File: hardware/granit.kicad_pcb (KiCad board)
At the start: 4 copper layers, 92 x 100 mm, 112 parts, among them IC1 ASM1061, J1 12V Barrel, J2 12V Screw Terminal, J3 RJ45_RB1-125B8G1A, J6 Conn_01x02, J7 USB_C_Receptacle_USB2.0_14P, J8 Conn_01x03, J9 SATA_22pin, Q1 FDS4435BZ, Q2 FDS4435BZ, Q3 FDS4435BZ, Q4 2N7002, Q5 2N7002, Q6 2N7002, SW1 SW_Push, U1 NCP1117-3.3_SOT223, U2 AP64501SP-13, U3 74AHCT1G125, U4 DS3231MZ, U5 USBLC6-2SC6, U6 74AHCT1G32, Y1 Crystal

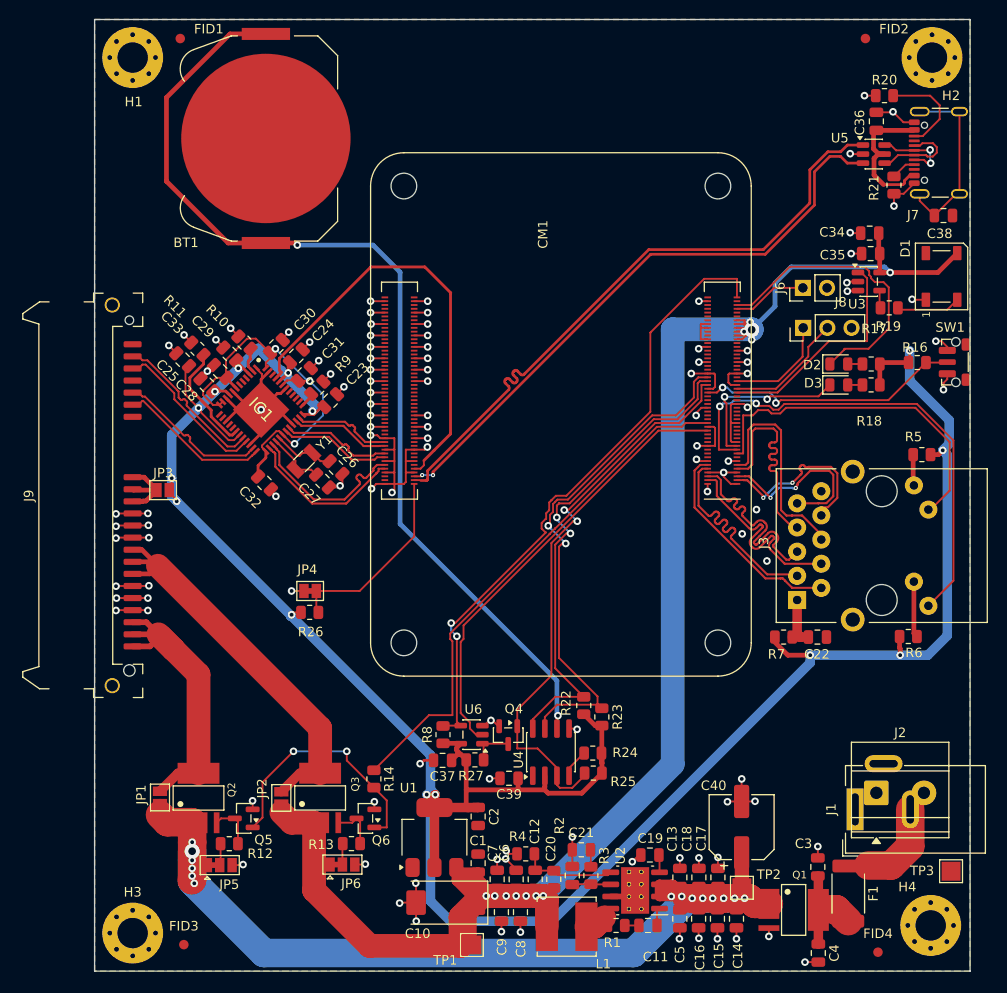
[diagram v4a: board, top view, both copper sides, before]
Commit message: Add comments to DRC exclusions
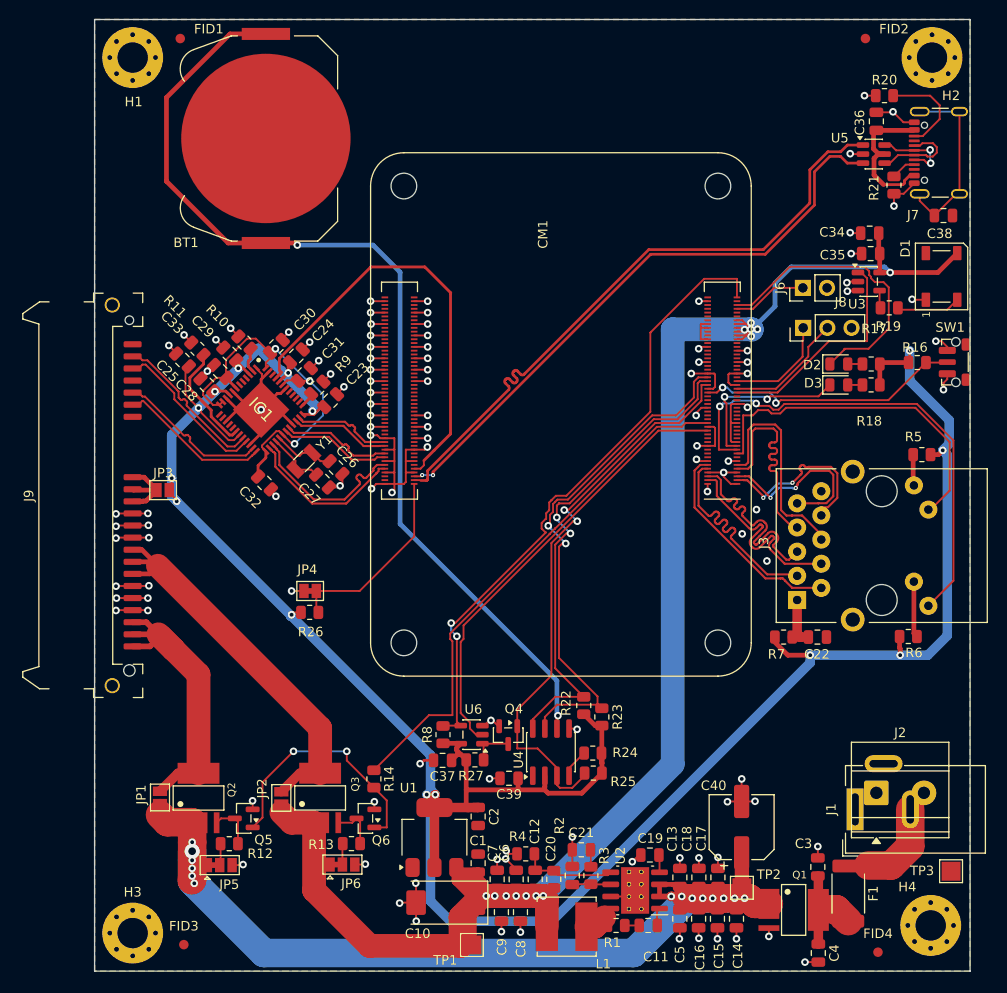
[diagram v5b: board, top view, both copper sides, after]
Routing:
- net +12VP: track 102.6 -> 96.7 mm
- net +5VP: track 190.0 -> 188.5 mm, vias 12 -> 13
- net GND: track 212.0 -> 212.9 mm
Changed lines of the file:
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@@
 	(footprint "Capacitor_SMD:C_0805_2012Metric"
 		(layer "F.Cu")
-		(at 29.25 55.75 135)
+		(at 29.23 55.78 135)
 		(descr "Capacitor SMD 0805 (2012 Metric), square (rectangular) end terminal, IPC-7351 nominal, (Body size source: IPC-SM-782 page 76, https://www.pcb-3d.com/wordpress/wp-content/uploads/ipc-sm-782a_amendment_1_and_2.pdf, https://docs.google.com/spreadsheets/d/1BsfQQcO9C6DZCsRaXUlFlo91Tg2WpOkGARC1WS5S8t0/edit?usp=sharing)")
 		(tags "capacitor")
@@
 	(footprint "Capacitor_SMD:C_0805_2012Metric"
 		(layer "F.Cu")
-		(at 78.15 115.199999)
+		(at 78.18 115.199999)
 		(descr "Capacitor SMD 0805 (2012 Metric), square (rectangular) end terminal, IPC-7351 nominal, (Body size source: IPC-SM-782 page 76, https://www.pcb-3d.com/wordpress/wp-content/uploads/ipc-sm-782a_amendment_1_and_2.pdf, https://docs.google.com/spreadsheets/d/1BsfQQcO9C6DZCsRaXUlFlo91Tg2WpOkGARC1WS5S8t0/edit?usp=sharing)")
 		(tags "capacitor")
@@
 	)
 	(segment
+		(start 76.165 112.154106)
+		(end 76.8 111.519106)
+		(width 0.2)
+		(layer "F.Cu")
+		(net "GND")
+	)
+	(segment
 		(start 83.675344 54.4)
 		(end 83.479024 54.59632)
@@
 	)
 	(segment
+		(start 74.2375 112.154106)
+		(end 76.165 112.154106)
+		(width 0.2)
+		(layer "F.Cu")
+		(net "GND")
+	)
+	(segment
 		(start 52.7 66.4)
 		(end 53.58 66.4)
@@
 	)
 	(segment
-		(start 74.2375 112.154106)
-		(end 76.165 112.154106)
-		(width 0.6)
-		(layer "F.Cu")
-		(net "GND")
-	)
-	(segment
 		(start 99.45 42.45)
 		(end 99.4 42.4)
@@
 	)
 	(segment
-		(start 88.3 52.1)
-		(end 88.8 52.6)
-		(width 0.2)
-		(layer "F.Cu")
-		(net "+5VP")
-	)
-	(segment
 		(start 88.425 53.225)
-		(end 89.05 52.6)
+		(end 88.825 52.825)
 		(width 0.2)
 		(layer "F.Cu")
@@
 	)
 	(segment
-		(start 87.5 51.6)
-		(end 88.3 51.6)
+		(start 88.975 52.675)
+		(end 89.05 52.6)
 		(width 0.2)
 		(layer "F.Cu")
@@
 	)
 	(segment
-		(start 88.2 52)
-		(end 88.3 52.1)
-		(width 0.2)
+		(start 64.05 112.1)
+		(end 61.15 112.1)
+		(width 2.5)
 		(layer "F.Cu")
 		(net "+5VP")
 	)
 	(segment
-		(start 64.05 112.1)
-		(end 61.15 112.1)
-		(width 2.5)
+		(start 88.05 51.6)
+		(end 88.45 52)
+		(width 0.2)
 		(layer "F.Cu")
 		(net "+5VP")
@@
 	)
 	(segment
+		(start 87.5 52)
+		(end 88.45 52)
+		(width 0.2)
+		(layer "F.Cu")
+		(net "+5VP")
+	)
+	(segment
 		(start 63.25 112.1)
 		(end 62.05 112.1)
@@
 	)
 	(segment
-		(start 87.5 52.4)
-		(end 88.45 52.4)
-		(width 0.2)
-		(layer "F.Cu")
-		(net "+5VP")
-	)
-	(segment
 		(start 103.6 46.587501)
 		(end 108.612499 46.587501)
@@
 	(segment
 		(start 88.85 52.8)
-		(end 89.05 52.6)
+		(end 88.975 52.675)
 		(width 0.2)
 		(layer "F.Cu")
@@
 	)
 	(segment
+		(start 88.1 52.8)
+		(end 88.3 52.6)
+		(width 0.2)
+		(layer "F.Cu")
+		(net "+5VP")
+	)
+	(segment
+		(start 88.1 52.4)
+		(end 88.3 52.6)
+		(width 0.2)
+		(layer "F.Cu")
+		(net "+5VP")
+	)
+	(segment
 		(start 60.02 109.879999)
 		(end 60.3 109.599999)
@@
 	)
 	(segment
-		(start 87.5 52)
-		(end 88.2 52)
-		(width 0.2)
-		(layer "F.Cu")
-		(net "+5VP")
-	)
-	(segment
 		(start 60.02 111.15)
 		(end 60.02 109.879999)
@@
 	)
 	(segment
-		(start 88.8 52.6)
-		(end 89.05 52.6)
-		(width 0.2)
-		(layer "F.Cu")
-		(net "+5VP")
-	)
-	(segment
 		(start 43.065 104.4)
 		(end 40.7 104.4)
@@
 	)
 	(segment
-		(start 87.5 52.8)
-		(end 88.85 52.8)
-		(width 0.2)
-		(layer "F.Cu")
-		(net "+5VP")
-	)
-	(segment
 		(start 102.499999 46.575002)
 		(end 102.499999 44.6)
@@
 	)
 	(segment
-		(start 88.3 51.6)
-		(end 88.3 51.85)
+		(start 87.5 53.2)
+		(end 88.45 53.2)
 		(width 0.2)
 		(layer "F.Cu")
@@
 	)
 	(segment
-		(start 87.5 53.2)
-		(end 88.45 53.2)
+		(start 88.825 52.825)
+		(end 89.05 52.6)
 		(width 0.2)
 		(layer "F.Cu")
@@
 	)
 	(segment
-		(start 88.3 51.85)
+		(start 87.5 52.4)
+		(end 88.1 52.4)
+		(width 0.2)
+		(layer "F.Cu")
+		(net "+5VP")
+	)
+	(segment
+		(start 88.45 52)
 		(end 89.05 52.6)
 		(width 0.2)
@@
 	)
 	(segment
+		(start 87.5 51.6)
+		(end 88.05 51.6)
+		(width 0.2)
+		(layer "F.Cu")
+		(net "+5VP")
+	)
+	(segment
+		(start 87.5 52.8)
+		(end 88.1 52.8)
+		(width 0.2)
+		(layer "F.Cu")
+		(net "+5VP")
+	)
+	(segment
 		(start 102.399999 42.45)
 		(end 102.399999 44.5)
@@
 	)
 	(via
-		(at 89.05 52.6)
-		(size 1.6)
-		(drill 0.8)
-		(layers "F.Cu" "B.Cu")
-		(net "+5VP")
-	)
-	(via
-		(at 88.9 51.8)
+		(at 88.975 51.875)
 		(size 0.8)
 		(drill 0.4)
@@
 	)
 	(via
-		(at 88.25 52.8)
+		(at 88.3 52.6)
 		(size 0.8)
 		(drill 0.4)
@@
 	)
 	(via
+		(at 88.95 52.55)
+		(size 0.8)
+		(drill 0.4)
+		(layers "F.Cu" "B.Cu")
+		(net "+5VP")
+	)
+	(via
 		(at 63.25 112.1)
 		(size 0.8)
@@
 	)
 	(via
-		(at 89.05 53.650003)
+		(at 89.65 52.55)
+		(size 0.8)
+		(drill 0.4)
+		(layers "F.Cu" "B.Cu")
+		(net "+5VP")
+	)
+	(via
+		(at 89 53.3)
 		(size 0.8)
 		(drill 0.4)
@@
 	)
 	(segment
+		(start 89.6 52.05)
+		(end 91.5 50.15)
+		(width 0.5)
+		(layer "B.Cu")
+		(net "+5VP")
+	)
+	(segment
 		(start 93.2 46)
 		(end 103.012499 46)
@@
 	(segment
 		(start 89.05 52.6)
-		(end 91.5 50.15)
+		(end 89.6 52.05)
 		(width 0.5)
 		(layer "B.Cu")
@@
 	)
 	(segment
+		(start 88.95 52.55)
+		(end 89.05 52.55)
+		(width 2.5)
+		(layer "B.Cu")
+		(net "+5VP")
+	)
+	(segment
 		(start 103.012499 46)
 		(end 103.6 46.587501)
@@
 	(segment
 		(start 80.75 52.55)
-		(end 89.05 52.55)
+		(end 88.95 52.55)
 		(width 2.5)
 		(layer "B.Cu")
@@
 	(segment
 		(start 80.784106 110.884106)
-		(end 81.2 111.3)
-		(width 1)
+		(end 82.25 112.35)
+		(width 0.5)
 		(layer "F.Cu")
 		(net "+12VP")
@@
 	)
 	(segment
-		(start 80.6325 110.884106)
-		(end 80.784106 110.884106)
-		(width 1)
-		(layer "F.Cu")
-		(net "+12VP")
-	)
-	(segment
-		(start 79.3625 110.884106)
-		(end 79.3625 112.154106)
-		(width 1)
-		(layer "F.Cu")
-		(net "+12VP")
-	)
-	(segment
 		(start 30.2275 104.35)
 		(end 30.285 104.4075)
@@
 	)
 	(segment
-		(start 81.2 111.521606)
-		(end 81.2 111.3)
-		(width 1)
-		(layer "F.Cu")
-		(net "+12VP")
-	)
-	(segment
-		(start 79.3625 110.884106)
-		(end 80.6325 110.884106)
-		(width 1)
-		(layer "F.Cu")
-		(net "+12VP")
-	)
-	(segment
 		(start 82.8 112.35)
 		(end 82.25 112.35)
@@
 	)
 	(segment
-		(start 80.6 112.121606)
-		(end 81.2 111.521606)
-		(width 1)
+		(start 79.3625 110.884106)
+		(end 79.3625 112.154106)
+		(width 0.5)
 		(layer "F.Cu")
 		(net "+12VP")
@@
 	)
 	(segment
-		(start 79.3625 112.154106)
-		(end 79.45 112.154106)
-		(width 1)
-		(layer "F.Cu")
-		(net "+12VP")
-	)
-	(segment
 		(start 30.25 110.4)
 		(end 30.25 110)
@@
 	)
 	(segment
-		(start 79.3625 112.154106)
-		(end 80.6325 110.884106)
-		(width 1)
-		(layer "F.Cu")
-		(net "+12VP")
-	)
-	(segment
 		(start 86.1 112.35)
 		(end 84.95 112.35)
@@
 	)
 	(segment
-		(start 81.2 111.3)
-		(end 82.25 112.35)
-		(width 1)
-		(layer "F.Cu")
-		(net "+12VP")
-	)
-	(segment
 		(start 80.6 112.121606)
 		(end 80.6 112.154106)
@@
 	(segment
 		(start 79.3625 110.884106)
-		(end 80.6 112.121606)
-		(width 1)
-		(layer "F.Cu")
-		(net "+12VP")
-	)
-	(segment
-		(start 79.45 112.154106)
-		(end 80.6 112.154106)
-		(width 1)
+		(end 80.784106 110.884106)
+		(width 0.5)
 		(layer "F.Cu")
 		(net "+12VP")

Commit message: Connect mounting holes H1-H4 to GND
- Change symbols from MountingHole to MountingHole_Pad
- Wire pad to GND for chassis ground through metal standoffs
- Update PCB from schematic to sync nets and fields
- ERC clean, 0 schematic parity issues
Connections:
- H1 pad 1: (no net) -> GND
- H2 pad 1: (no net) -> GND
- H3 pad 1: (no net) -> GND
- H4 pad 1: (no net) -> GND
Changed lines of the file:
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@@
 			)
 		)
-		(property "Description" "Mounting Hole without connection"
+		(property "Description" "Mounting Hole with connection"
 			(at 0 0 0)
 			(layer "F.Fab")
@@
 			)
 		)
-		(property ki_fp_filters "MountingHole*")
+		(property ki_fp_filters "MountingHole*Pad*")
 		(sheetname "/")
 		(sheetfile "granit.kicad_sch")
+		(units
+			(unit
+				(name "A")
+				(pins "1")
+			)
+		)
 		(attr exclude_from_bom)
 		(duplicate_pad_numbers_are_jumpers no)
@@
 			(layers "*.Cu" "*.Mask")
 			(remove_unused_layers no)
+			(net "GND")
+			(pinfunction "1_1")
+			(pintype "input")
 			(zone_connect 2)
 		)
@@
 			(layers "*.Cu" "*.Mask")
 			(remove_unused_layers no)
+			(net "GND")
+			(pinfunction "1_1")
+			(pintype "input")
 			(zone_connect 2)
 		)
@@
 			(layers "*.Cu" "*.Mask")
 			(remove_unused_layers no)
+			(net "GND")
+			(pinfunction "1_1")
+			(pintype "input")
 			(zone_connect 2)
 		)
@@
 			(layers "*.Cu" "*.Mask")
 			(remove_unused_layers no)
+			(net "GND")
+			(pinfunction "1_1")
+			(pintype "input")
 			(zone_connect 2)
 		)
@@
 			(layers "*.Cu" "*.Mask")
 			(remove_unused_layers no)
+			(net "GND")
+			(pinfunction "1_1")
+			(pintype "input")
 			(zone_connect 2)
 		)
@@
 			(layers "*.Cu" "*.Mask")
 			(remove_unused_layers no)
+			(net "GND")
+			(pinfunction "1_1")
+			(pintype "input")
 			(zone_connect 2)
 		)
@@
 			(layers "*.Cu" "*.Mask")
 			(remove_unused_layers no)
+			(net "GND")
+			(pinfunction "1_1")
+			(pintype "input")
 			(zone_connect 2)
 		)
@@
 			(layers "*.Cu" "*.Mask")
 			(remove_unused_layers no)
+			(net "GND")
+			(pinfunction "1_1")
+			(pintype "input")
 			(zone_connect 2)
 		)
@@
 			(layers "*.Cu" "*.Mask")
 			(remove_unused_layers no)
+			(net "GND")
+			(pinfunction "1_1")
+			(pintype "input")
 			(zone_connect 2)
 		)
@@
 			)
 		)
-		(property "Description" "Mounting Hole without connection"
+		(property "Description" "Mounting Hole with connection"
 			(at 0 0 0)
 			(layer "F.Fab")
@@
 			)
 		)
-		(property ki_fp_filters "MountingHole*")
+		(property ki_fp_filters "MountingHole*Pad*")
 		(sheetname "/")
 		(sheetfile "granit.kicad_sch")
+		(units
+			(unit
+				(name "A")
+				(pins "1")
+			)
+		)
 		(attr exclude_from_bom)
 		(duplicate_pad_numbers_are_jumpers no)
@@
 			(layers "*.Cu" "*.Mask")
 			(remove_unused_layers no)
+			(net "GND")
+			(pinfunction "1_1")
+			(pintype "input")
 			(zone_connect 2)
 		)
@@
 			(layers "*.Cu" "*.Mask")
 			(remove_unused_layers no)
+			(net "GND")
+			(pinfunction "1_1")
+			(pintype "input")
 			(zone_connect 2)
 		)
@@
 			(layers "*.Cu" "*.Mask")
 			(remove_unused_layers no)
+			(net "GND")
+			(pinfunction "1_1")
+			(pintype "input")
 			(zone_connect 2)
 		)
@@
 			(layers "*.Cu" "*.Mask")
 			(remove_unused_layers no)
+			(net "GND")
+			(pinfunction "1_1")
+			(pintype "input")
 			(zone_connect 2)
 		)
@@
 			(layers "*.Cu" "*.Mask")
 			(remove_unused_layers no)
+			(net "GND")
+			(pinfunction "1_1")
+			(pintype "input")
 			(zone_connect 2)
 		)
@@
 			(layers "*.Cu" "*.Mask")
 			(remove_unused_layers no)
+			(net "GND")
+			(pinfunction "1_1")
+			(pintype "input")
 			(zone_connect 2)
 		)
@@
 			(layers "*.Cu" "*.Mask")
 			(remove_unused_layers no)
+			(net "GND")
+			(pinfunction "1_1")
+			(pintype "input")
 			(zone_connect 2)
 		)
@@
 			(layers "*.Cu" "*.Mask")
 			(remove_unused_layers no)
+			(net "GND")
+			(pinfunction "1_1")
+			(pintype "input")
 			(zone_connect 2)
 		)
@@
 			(layers "*.Cu" "*.Mask")
 			(remove_unused_layers no)
+			(net "GND")
+			(pinfunction "1_1")
+			(pintype "input")
 			(zone_connect 2)
 		)
@@
 			)
 		)
-		(property "Description" "Mounting Hole without connection"
+		(property "Description" "Mounting Hole with connection"
 			(at 0 0 0)
 			(layer "F.Fab")
@@
 			)
 		)
-		(property ki_fp_filters "MountingHole*")
+		(property ki_fp_filters "MountingHole*Pad*")
 		(sheetname "/")
 		(sheetfile "granit.kicad_sch")
+		(units
+			(unit
+				(name "A")
+				(pins "1")
+			)
+		)
 		(attr exclude_from_bom)
 		(duplicate_pad_numbers_are_jumpers no)
@@
 			(layers "*.Cu" "*.Mask")
 			(remove_unused_layers no)
+			(net "GND")
+			(pinfunction "1_1")
+			(pintype "input")
 			(zone_connect 2)
 		)
@@
 			(layers "*.Cu" "*.Mask")
 			(remove_unused_layers no)
+			(net "GND")
+			(pinfunction "1_1")
+			(pintype "input")
 			(zone_connect 2)
 		)
@@
 			(layers "*.Cu" "*.Mask")
 			(remove_unused_layers no)
+			(net "GND")
+			(pinfunction "1_1")
+			(pintype "input")
 			(zone_connect 2)
 		)
@@
 			(layers "*.Cu" "*.Mask")
 			(remove_unused_layers no)
+			(net "GND")
+			(pinfunction "1_1")
+			(pintype "input")
 			(zone_connect 2)
 		)
@@
 			(layers "*.Cu" "*.Mask")
 			(remove_unused_layers no)
+			(net "GND")
+			(pinfunction "1_1")
+			(pintype "input")
 			(zone_connect 2)
 		)
@@
 			(layers "*.Cu" "*.Mask")
 			(remove_unused_layers no)
+			(net "GND")
+			(pinfunction "1_1")
+			(pintype "input")
 			(zone_connect 2)
 		)
@@
 			(layers "*.Cu" "*.Mask")
 			(remove_unused_layers no)
+			(net "GND")
+			(pinfunction "1_1")
+			(pintype "input")
 			(zone_connect 2)
 		)
@@
 			(layers "*.Cu" "*.Mask")
 			(remove_unused_layers no)
+			(net "GND")
+			(pinfunction "1_1")
+			(pintype "input")
 			(zone_connect 2)
 		)
@@
 			(layers "*.Cu" "*.Mask")
 			(remove_unused_layers no)
+			(net "GND")
+			(pinfunction "1_1")
+			(pintype "input")
 			(zone_connect 2)
 		)
@@
 			)
 		)
-		(property "Description" "Mounting Hole without connection"
+		(property "Description" "Mounting Hole with connection"
 			(at 0 0 0)
 			(layer "F.Fab")
@@
 			)
 		)
-		(property ki_fp_filters "MountingHole*")
+		(property ki_fp_filters "MountingHole*Pad*")
 		(sheetname "/")
 		(sheetfile "granit.kicad_sch")
+		(units
+			(unit
+				(name "A")
+				(pins "1")
+			)
+		)
 		(attr exclude_from_bom)
 		(duplicate_pad_numbers_are_jumpers no)
@@
 			(layers "*.Cu" "*.Mask")
 			(remove_unused_layers no)
+			(net "GND")
+			(pinfunction "1_1")
+			(pintype "input")
 			(zone_connect 2)
 		)
@@
 			(layers "*.Cu" "*.Mask")
 			(remove_unused_layers no)
+			(net "GND")
+			(pinfunction "1_1")
+			(pintype "input")
 			(zone_connect 2)
 		)
@@
 			(layers "*.Cu" "*.Mask")
 			(remove_unused_layers no)
+			(net "GND")
+			(pinfunction "1_1")
+			(pintype "input")
 			(zone_connect 2)
 		)
@@
 			(layers "*.Cu" "*.Mask")
 			(remove_unused_layers no)
+			(net "GND")
+			(pinfunction "1_1")
+			(pintype "input")
 			(zone_connect 2)
 		)
@@
 			(layers "*.Cu" "*.Mask")
 			(remove_unused_layers no)
+			(net "GND")
+			(pinfunction "1_1")
+			(pintype "input")
 			(zone_connect 2)
 		)
@@
 			(layers "*.Cu" "*.Mask")
 			(remove_unused_layers no)
+			(net "GND")
+			(pinfunction "1_1")
+			(pintype "input")
 			(zone_connect 2)
 		)
@@
 			(layers "*.Cu" "*.Mask")
 			(remove_unused_layers no)
+			(net "GND")
+			(pinfunction "1_1")
+			(pintype "input")
 			(zone_connect 2)
 		)
@@
 			(layers "*.Cu" "*.Mask")
 			(remove_unused_layers no)
+			(net "GND")
+			(pinfunction "1_1")
+			(pintype "input")
 			(zone_connect 2)
 		)
@@
 			(layers "*.Cu" "*.Mask")
 			(remove_unused_layers no)
+			(net "GND")
+			(pinfunction "1_1")
+			(pintype "input")
 			(zone_connect 2)
 		)
